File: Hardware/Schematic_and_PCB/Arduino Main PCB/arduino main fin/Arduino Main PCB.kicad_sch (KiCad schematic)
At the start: 82 parts, among them J1 PIR_sensor, J10 LED_Room_2, J11 LED_Room_3, J12 LED_DOOR, J13 Buttons_Room_2, J14 Barrel_Jack, J15 Power switch, J2 Control_Panel, J3 Buttons_Room_3, J4 Buttons_Room_1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

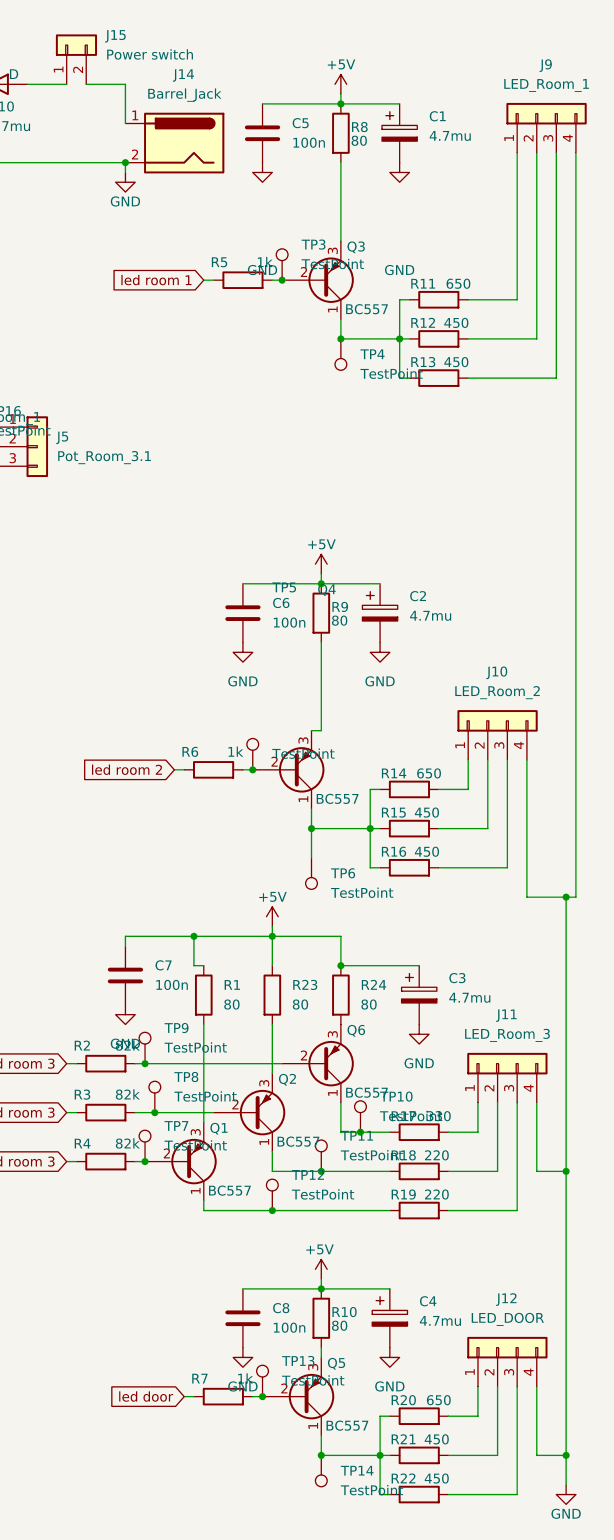
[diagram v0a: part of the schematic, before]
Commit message: Schematic of main PCB updated with Resistor values
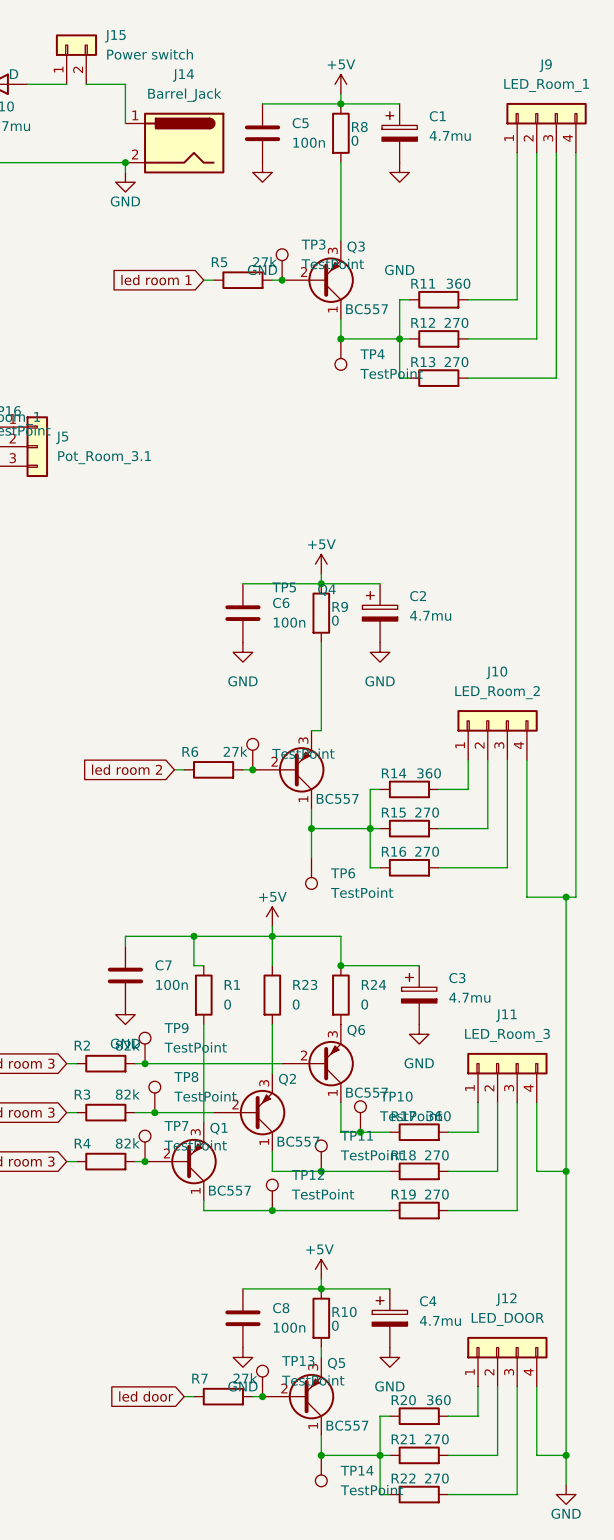
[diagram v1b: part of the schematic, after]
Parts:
- R1, R10, R23, R24, R8, R9: value 80 -> 0
- R11, R14, R20: value 650 -> 360
- R12, R13, R15, R16, R21, R22: value 450 -> 270
- R17: value 330 -> 360
- R18, R19: value 220 -> 270
- R5, R6, R7: value 1k -> 27k
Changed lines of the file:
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@@
 			)
 		)
-		(property "Value" "650"
+		(property "Value" "360"
 			(at 181.61 193.548 90)
 			(effects
@@
 			)
 		)
-		(property "Value" "450"
+		(property "Value" "270"
 			(at 180.086 122.428 90)
 			(effects
@@
 			)
 		)
-		(property "Value" "80"
+		(property "Value" "0"
 			(at 153.67 142.2399 0)
 			(effects
@@
 			)
 		)
-		(property "Value" "80"
+		(property "Value" "0"
 			(at 171.45 142.2399 0)
 			(effects
@@
 			)
 		)
-		(property "Value" "450"
+		(property "Value" "270"
 			(at 183.896 58.928 90)
 			(effects
@@
 			)
 		)
-		(property "Value" "80"
+		(property "Value" "0"
 			(at 162.56 142.2399 0)
 			(effects
@@
 			)
 		)
-		(property "Value" "450"
+		(property "Value" "270"
 			(at 183.896 53.848 90)
 			(effects
@@
 			)
 		)
-		(property "Value" "450"
+		(property "Value" "270"
 			(at 181.356 198.628 90)
 			(effects
@@
 			)
 		)
-		(property "Value" "450"
+		(property "Value" "270"
 			(at 180.086 117.348 90)
 			(effects
@@
 			)
 		)
-		(property "Value" "650"
+		(property "Value" "360"
 			(at 184.15 48.768 90)
 			(effects
@@
 			)
 		)
-		(property "Value" "220"
+		(property "Value" "270"
 			(at 181.356 166.878 90)
 			(effects
@@
 			)
 		)
-		(property "Value" "80"
+		(property "Value" "0"
 			(at 170.18 30.226 0)
 			(effects
@@
 			)
 		)
-		(property "Value" "330"
+		(property "Value" "360"
 			(at 181.61 156.718 90)
 			(effects
@@
 			)
 		)
-		(property "Value" "80"
+		(property "Value" "0"
 			(at 167.64 92.456 0)
 			(effects
@@
 			)
 		)
-		(property "Value" "1k"
+		(property "Value" "27k"
 			(at 159.004 45.974 90)
 			(effects
@@
 			)
 		)
-		(property "Value" "650"
+		(property "Value" "360"
 			(at 180.34 112.268 90)
 			(effects
@@
 			)
 		)
-		(property "Value" "450"
+		(property "Value" "270"
 			(at 181.356 203.708 90)
 			(effects
@@
 			)
 		)
-		(property "Value" "220"
+		(property "Value" "270"
 			(at 181.356 161.798 90)
 			(effects
@@
 			)
 		)
-		(property "Value" "80"
+		(property "Value" "0"
 			(at 167.64 183.896 0)
 			(effects
@@
 			)
 		)
-		(property "Value" "1k"
+		(property "Value" "27k"
 			(at 156.464 190.754 90)
 			(effects
@@
 			)
 		)
-		(property "Value" "1k"
+		(property "Value" "27k"
 			(at 155.194 109.474 90)
 			(effects

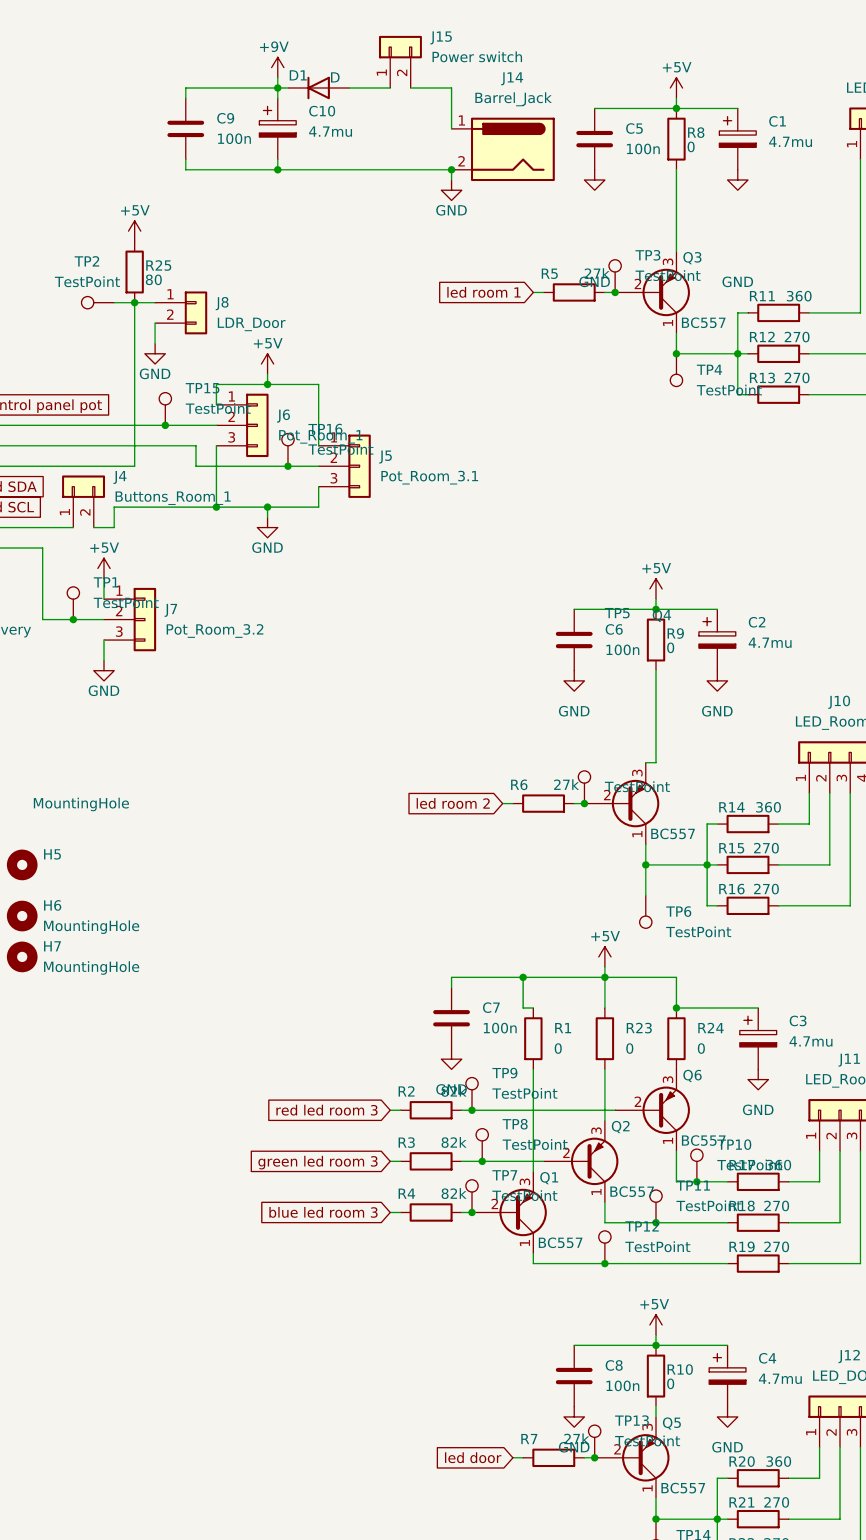
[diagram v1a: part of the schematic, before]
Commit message: updated arduino main schematic
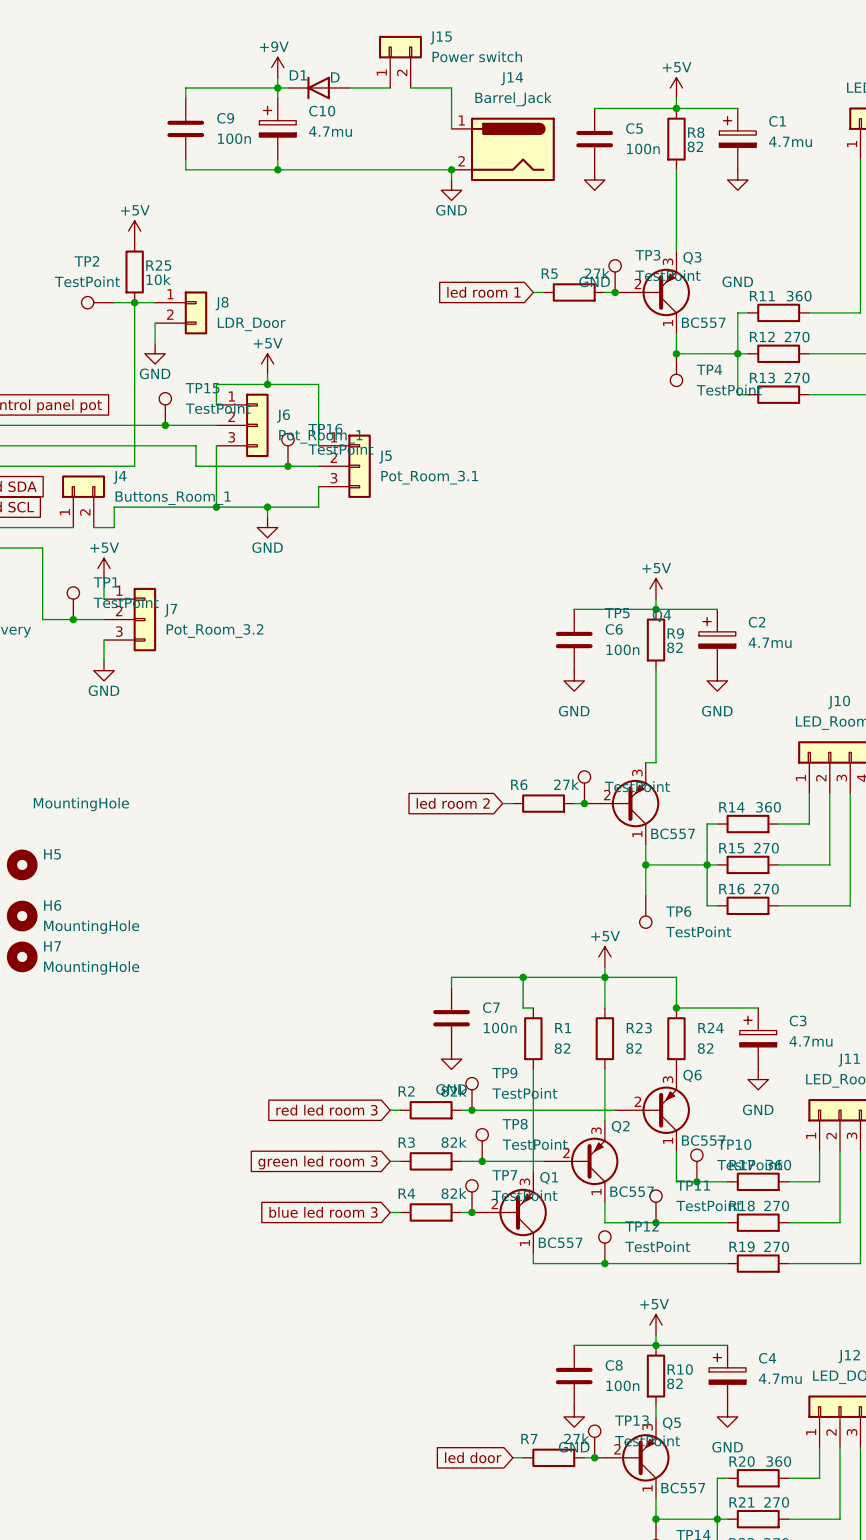
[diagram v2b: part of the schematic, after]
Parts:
- R1, R10, R23, R24, R8, R9: value 0 -> 82
- R25: value 80 -> 10k
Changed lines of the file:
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@@
 			)
 		)
-		(property "Value" "0"
+		(property "Value" "82"
 			(at 153.67 142.2399 0)
 			(effects
@@
 			)
 		)
-		(property "Value" "0"
+		(property "Value" "82"
 			(at 171.45 142.2399 0)
 			(effects
@@
 			)
 		)
-		(property "Value" "0"
+		(property "Value" "82"
 			(at 162.56 142.2399 0)
 			(effects
@@
 			)
 		)
-		(property "Value" "0"
+		(property "Value" "82"
 			(at 170.18 30.226 0)
 			(effects
@@
 			)
 		)
-		(property "Value" "0"
+		(property "Value" "82"
 			(at 167.64 92.456 0)
 			(effects
@@
 			)
 		)
-		(property "Value" "0"
+		(property "Value" "82"
 			(at 167.64 183.896 0)
 			(effects
@@
 			)
 		)
-		(property "Value" "80"
+		(property "Value" "10k"
 			(at 102.87 46.736 0)
 			(effects

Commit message: Make schematic more readable.
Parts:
- C1, C2, C3, C4: value 4.7mu -> 4u7
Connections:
- net GND: no longer J11.4 (Pin_4)
- net at Q3.1 (C), R12.1, R13.1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: no longer R11.1
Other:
- note added: "Control panel connection"
- note added: "LED connections"
- note added: "Main Arduino connections"
- note added: "Mounting holes for Arduino PCB"
- note added: "Mounting holes for Control panel"
- note added: "Power supply"
- title: (none) -> Main PCB
- moved on the sheet: A1, C1, C10, C2, C3, C4, C5, C6, C7, C8, C9, D1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
